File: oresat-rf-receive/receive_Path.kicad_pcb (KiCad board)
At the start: 4 copper layers, 26 x 60.3 mm, 32 parts, among them J1 Conn_Coaxial_142-0711-201, J2 Conn_Coaxial_142-0711-201, J3 0022232021, J4 0022232041, J5 0022232021, U1 TQP3M9037, U2 PAT1220-C-3DB, U3 SN74LVC1G32QDBVRQ1, U4 PAT1220-C-3DB, U5 TQP3M9037, U6 PD2328J5050S2HF, U7 LTC5505-1ES5

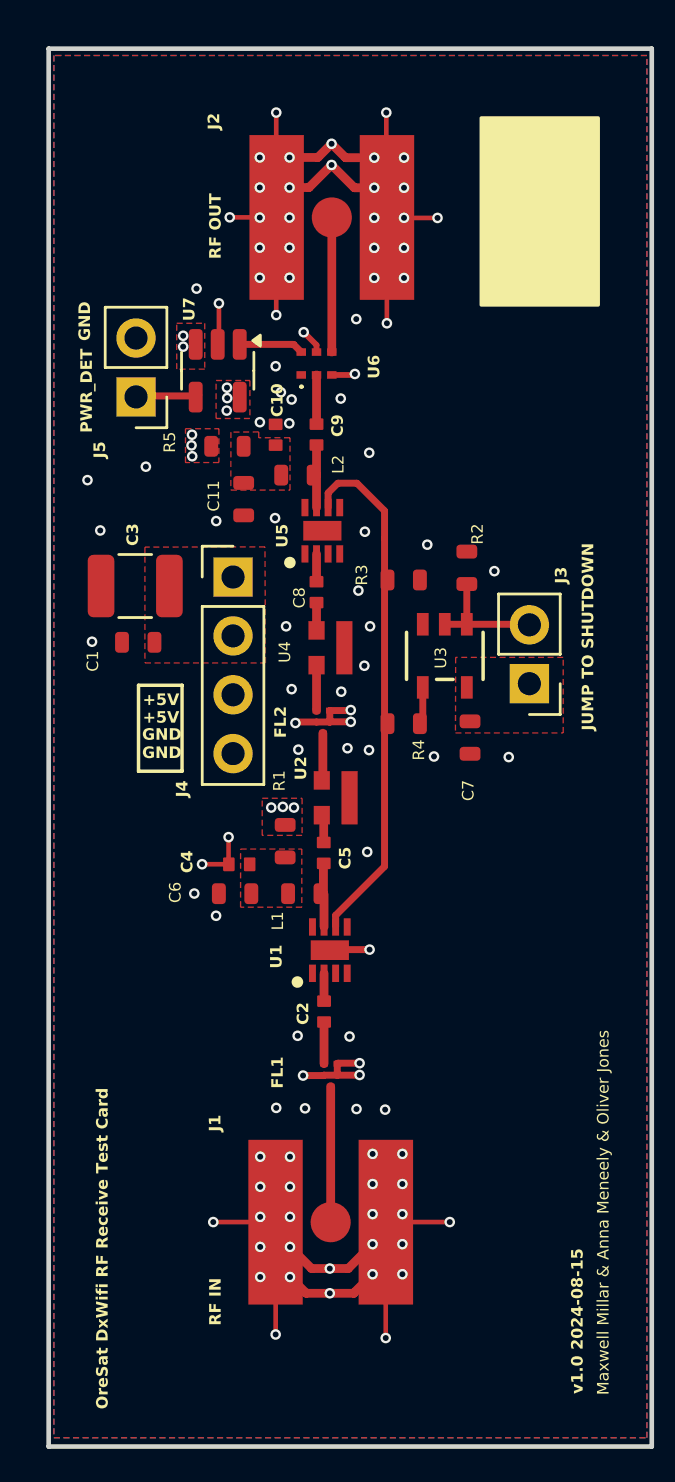
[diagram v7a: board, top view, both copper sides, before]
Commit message: fixed connector reference designators and BOM for receive test board
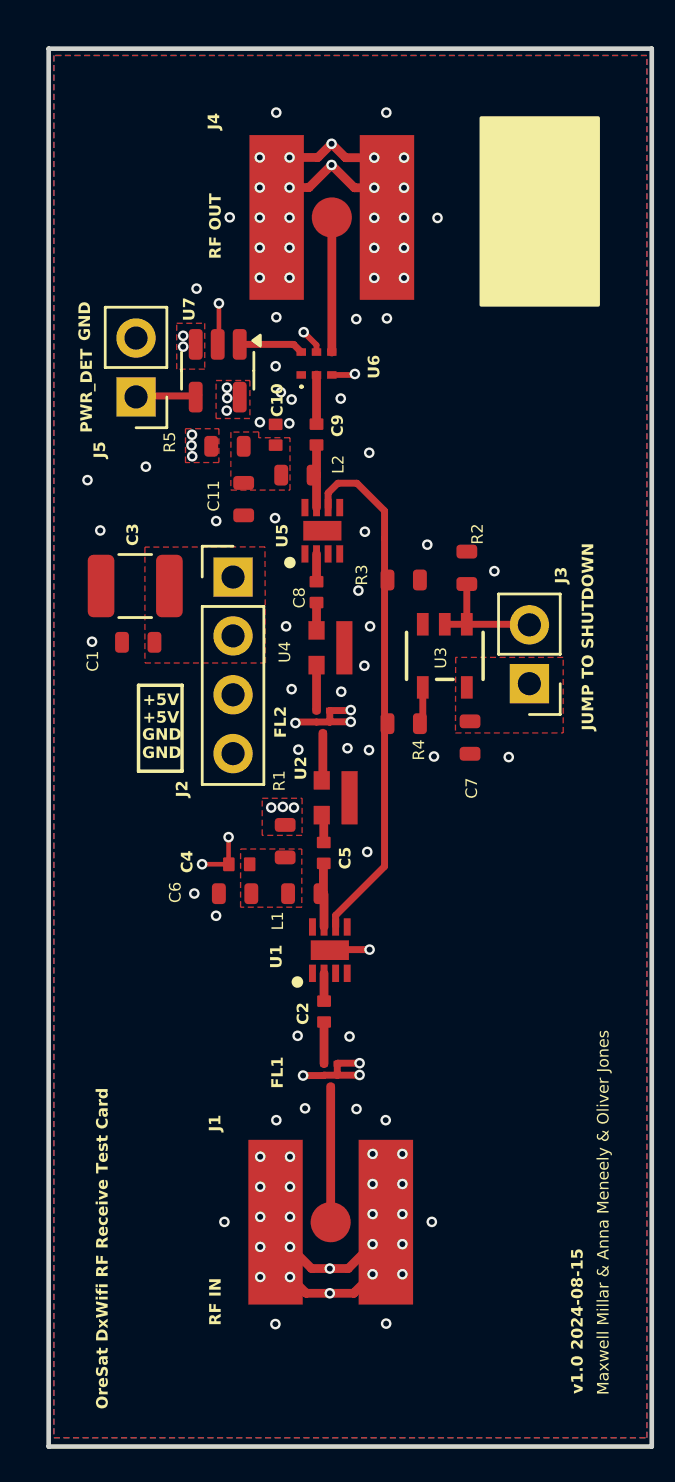
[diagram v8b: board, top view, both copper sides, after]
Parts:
- renumbered J4 to J2, J2 to J4
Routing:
- net GND: track 70.5 -> 33.7 mm
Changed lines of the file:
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@@
 		(descr "142-0711-201")
 		(tags "Connector")
-		(property "Reference" "J2"
+		(property "Reference" "J4"
 			(at 5.09055 4.1441 90)
 			(unlocked yes)
@@
 		(descr "<b>0603 (metric 1608) tight 'IPC-C' without silkscreen</b>\n<br>In house package for minimum spacing based on IPC-7351B.\nThis package is identical to 0603-C, but has its tPlace silkscreen layer removed.")
 		(property "Reference" "C7"
-			(at 2.74 -0.21 -90)
+			(at 2.64 -0.36 -90)
 			(layer "F.SilkS")
 			(effects
@@
 		(descr "Through hole straight pin header, 1x04, 2.54mm pitch, single row")
 		(tags "Through hole pin header THT 1x04 2.54mm single row")
-		(property "Reference" "J4"
+		(property "Reference" "J2"
 			(at -2.19975 9.1411 90)
 			(unlocked yes)
@@
 	)
 	(segment
-		(start 115.6716 95.3516)
-		(end 115.6716 90.78645)
-		(width 0.2)
-		(layer "F.Cu")
-		(net 1)
-	)
-	(segment
 		(start 110.91065 90.7796)
 		(end 110.91455 90.7835)
@@
 	)
 	(segment
-		(start 110.8964 94.996)
-		(end 110.8964 90.80165)
-		(width 0.2)
-		(layer "F.Cu")
-		(net 1)
-	)
-	(segment
 		(start 108.42255 94.4909)
 		(end 108.42255 96.20995)
@@
 	)
 	(segment
-		(start 115.6462 86.2584)
-		(end 115.6462 90.75515)
-		(width 0.2)
-		(layer "F.Cu")
-		(net 1)
-	)
-	(segment
 		(start 114.11215 112.5503)
 		(end 113.21475 112.5503)
@@
 	)
 	(segment
-		(start 110.8964 86.2584)
-		(end 110.8964 90.76535)
-		(width 0.2)
-		(layer "F.Cu")
-		(net 1)
-	)
-	(segment
 		(start 112.95955 127.7985)
 		(end 113.53155 127.7985)
@@
 	)
 	(segment
-		(start 115.6208 139.1412)
-		(end 115.6208 134.26575)
-		(width 0.2)
-		(layer "F.Cu")
-		(net 1)
-	)
-	(segment
 		(start 112.94555 122.1895)
 		(end 112.95955 122.2035)
@@
 	)
 	(segment
-		(start 110.871 139.0396)
-		(end 110.871 134.19975)
-		(width 0.2)
-		(layer "F.Cu")
-		(net 1)
-	)
-	(segment
 		(start 113.20655 112.5585)
 		(end 113.20655 112.0635)
@@
 	)
 	(segment
-		(start 118.383975 134.1374)
-		(end 115.651625 134.1374)
-		(width 0.2)
-		(layer "F.Cu")
-		(net 1)
-	)
-	(segment
 		(start 113.20655 112.0635)
 		(end 114.09095 112.0635)
@@
 	)
 	(segment
-		(start 117.856 90.805)
-		(end 115.69605 90.805)
-		(width 0.2)
-		(layer "F.Cu")
-		(net 1)
-	)
-	(segment
 		(start 113.2078 136.144)
 		(end 114.001 136.144)
@@
 	)
 	(segment
-		(start 108.8898 90.7796)
-		(end 110.91065 90.7796)
-		(width 0.2)
-		(layer "F.Cu")
-		(net 1)
-	)
-	(segment
 		(start 110.8964 90.76535)
 		(end 110.91455 90.7835)
@@
 	)
 	(segment
-		(start 108.1786 134.1374)
-		(end 110.68165 134.1374)
-		(width 0.2)
-		(layer "F.Cu")
-		(net 1)
-	)
-	(segment
 		(start 114.001 136.144)
 		(end 115.055 135.09)
@@
 	)
 	(via
-		(at 118.383975 134.1374)
+		(at 117.61 134.13)
 		(size 0.4572)
 		(drill 0.254)
@@
 	)
 	(via
-		(at 115.5954 129.286)
+		(at 115.62 129.74)
 		(size 0.4572)
 		(drill 0.254)
@@
 	)
 	(via
-		(at 108.1786 134.1374)
+		(at 108.66 134.13)
 		(size 0.4572)
 		(drill 0.254)
@@
 	)
 	(via
-		(at 110.8964 129.2098)
+		(at 110.9 129.74)
 		(size 0.4572)
 		(drill 0.254)
@@
 	)
 	(via
-		(at 110.8964 94.996)
+		(at 110.9 95.09)
 		(size 0.4572)
 		(drill 0.254)
@@
 	)
 	(via
-		(at 110.871 138.9888)
+		(at 110.86 138.54)
 		(size 0.4572)
 		(drill 0.254)
@@
 	)
 	(via
-		(at 115.6716 95.3516)
+		(at 115.6716 95.14)
 		(size 0.4572)
 		(drill 0.254)
@@
 	)
 	(via
-		(at 115.6208 139.1412)
+		(at 115.64 138.52)
 		(size 0.4572)
 		(drill 0.254)
